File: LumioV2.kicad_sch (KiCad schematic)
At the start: 56 parts, among them J1 I2C POINT 1 - QWIIC, J10 MOTOR B, J11 Analog Input, J12 Analog Input, J13 Analog Input, J14 Analog Input, J15 Analog Input, J16 Analog Input, J17 Analog Input, J18 Analog Input, J2 I2C POINT 2 - QWIIC, J3 I2C POINT 3 - JST-PH, J4 I2C POINT 4 - JST-PH, J5 Raspi 5, J6 US Dist - Front, J7 US Dist - Back, J8 Display Connector, J9 MOTOR A, U1 LM2577T-ADJ/NOPB, U2 L298N, U3 MCP3008

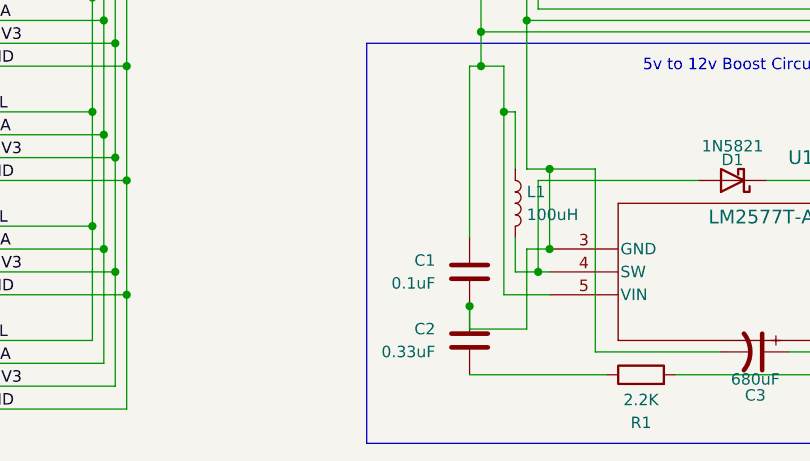
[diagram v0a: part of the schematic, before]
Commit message: added all footprints to schematics, also added all footprints to the pcb what's left: layout and routing
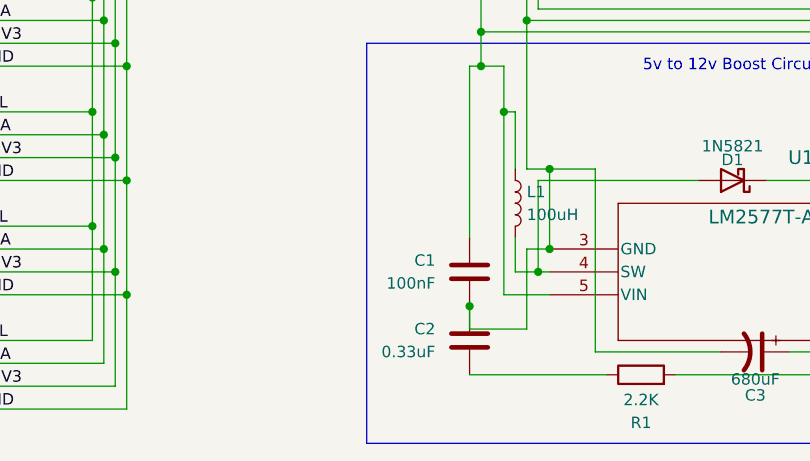
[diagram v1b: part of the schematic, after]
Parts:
- C1: value 0.1uF -> 100nF; footprint Capacitor_SMD:C_0603_1608Metric -> Capacitor_SMD:C_0402_1005Metric_Pad0.74x0.62mm_HandSolder
- C10, C11, C12, C13, C14, C15, C16, C17, C18, C19, C2, C20, C21, C22, C23, C24, C4, C5, C6, C7, C8, C9: footprint Capacitor_SMD:C_0603_1608Metric -> Capacitor_SMD:C_0402_1005Metric_Pad0.74x0.62mm_HandSolder
- D2, D3, D4, D5, D6, D7, D8, D9: value 1N4148WT -> SS34B; footprint Diode_SMD:D_SOD-523 -> Diode_SMD:D_SMA_Handsoldering
- J10, J9: footprint (none) -> TerminalBlock:TerminalBlock_MaiXu_MX126-5.0-02P_1x02_P5.00mm
- J11, J12, J13, J14, J15, J16, J17, J18: footprint (none) -> Connector_PinHeader_2.54mm:PinHeader_1x03_P2.54mm_Vertical
- J5: footprint Connector_PinHeader_1.00mm:PinHeader_2x20_P1.00mm_Vertical -> Connector_PinHeader_2.54mm:PinHeader_2x20_P2.54mm_Vertical
- J6, J7: footprint (none) -> Connector_PinHeader_2.54mm:PinHeader_1x04_P2.54mm_Vertical
- J8: footprint (none) -> Connector_PinHeader_2.54mm:PinHeader_2x13_P2.54mm_Vertical
- L1: footprint (none) -> Inductor_THT:L_Radial_D21.0mm_P19.00mm
- R1: footprint (none) -> Resistor_SMD:R_0805_2012Metric_Pad1.20x1.40mm_HandSolder
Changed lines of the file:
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@@
 			)
 		)
-		(property "Footprint" "Capacitor_SMD:C_0603_1608Metric"
+		(property "Footprint" "Capacitor_SMD:C_0402_1005Metric_Pad0.74x0.62mm_HandSolder"
 			(at 31.75 166.37 0)
 			(effects
@@
 			)
 		)
-		(property "Footprint" ""
+		(property "Footprint" "TerminalBlock:TerminalBlock_MaiXu_MX126-5.0-02P_1x02_P5.00mm"
 			(at 251.46 147.32 0)
 			(effects
@@
 			)
 		)
-		(property "Footprint" "Capacitor_SMD:C_0603_1608Metric"
+		(property "Footprint" "Capacitor_SMD:C_0402_1005Metric_Pad0.74x0.62mm_HandSolder"
 			(at 250.19 44.45 0)
 			(effects
@@
 			)
 		)
-		(property "Value" "1N4148WT"
+		(property "Value" "SS34B"
 			(at 243.84 139.7 90)
 			(effects
@@
 			)
 		)
-		(property "Footprint" "Diode_SMD:D_SOD-523"
+		(property "Footprint" "Diode_SMD:D_SMA_Handsoldering"
 			(at 234.315 132.08 0)
 			(effects
@@
 			)
 		)
-		(property "Footprint" "Capacitor_SMD:C_0603_1608Metric"
+		(property "Footprint" "Capacitor_SMD:C_0402_1005Metric_Pad0.74x0.62mm_HandSolder"
 			(at 101.6 31.75 0)
 			(effects
@@
 			)
 		)
-		(property "Footprint" "Capacitor_SMD:C_0603_1608Metric"
+		(property "Footprint" "Capacitor_SMD:C_0402_1005Metric_Pad0.74x0.62mm_HandSolder"
 			(at 199.0852 127 0)
 			(effects
@@
 			)
 		)
-		(property "Footprint" "Capacitor_SMD:C_0603_1608Metric"
+		(property "Footprint" "Capacitor_SMD:C_0402_1005Metric_Pad0.74x0.62mm_HandSolder"
 			(at 173.99 92.71 0)
 			(effects
@@
 			)
 		)
-		(property "Value" "1N4148WT"
+		(property "Value" "SS34B"
 			(at 238.76 165.1 90)
 			(effects
@@
 			)
 		)
-		(property "Footprint" "Diode_SMD:D_SOD-523"
+		(property "Footprint" "Diode_SMD:D_SMA_Handsoldering"
 			(at 229.235 157.48 0)
 			(effects
@@
 			)
 		)
-		(property "Value" "1N4148WT"
+		(property "Value" "SS34B"
 			(at 233.68 165.1 90)
 			(effects
@@
 			)
 		)
-		(property "Footprint" "Diode_SMD:D_SOD-523"
+		(property "Footprint" "Diode_SMD:D_SMA_Handsoldering"
 			(at 224.155 157.48 0)
 			(effects
@@
 			)
 		)
-		(property "Value" "0.1uF"
+		(property "Value" "100nF"
 			(at 101.6 177.7999 0)
 			(effects
@@
 			)
 		)
-		(property "Footprint" "Capacitor_SMD:C_0603_1608Metric"
+		(property "Footprint" "Capacitor_SMD:C_0402_1005Metric_Pad0.74x0.62mm_HandSolder"
 			(at 104.4448 180.34 0)
 			(effects
@@
 			)
 		)
-		(property "Footprint" ""
+		(property "Footprint" "Connector_PinHeader_2.54mm:PinHeader_1x03_P2.54mm_Vertical"
 			(at 241.3 54.61 0)
 			(effects
@@
 			)
 		)
-		(property "Footprint" "Connector_PinHeader_1.00mm:PinHeader_2x20_P1.00mm_Vertical"
+		(property "Footprint" "Connector_PinHeader_2.54mm:PinHeader_2x20_P2.54mm_Vertical"
 			(at 90.17 81.28 0)
 			(effects
@@
 			)
 		)
-		(property "Footprint" "Capacitor_SMD:C_0603_1608Metric"
+		(property "Footprint" "Capacitor_SMD:C_0402_1005Metric_Pad0.74x0.62mm_HandSolder"
 			(at 213.0552 127 0)
 			(effects
@@
 			)
 		)
-		(property "Footprint" "Capacitor_SMD:C_0603_1608Metric"
+		(property "Footprint" "Capacitor_SMD:C_0402_1005Metric_Pad0.74x0.62mm_HandSolder"
 			(at 31.75 191.77 0)
 			(effects
@@
 			)
 		)
-		(property "Footprint" ""
+		(property "Footprint" "Connector_PinHeader_2.54mm:PinHeader_1x03_P2.54mm_Vertical"
 			(at 227.33 39.37 0)
 			(effects
@@
 			)
 		)
-		(property "Footprint" "Capacitor_SMD:C_0603_1608Metric"
+		(property "Footprint" "Capacitor_SMD:C_0402_1005Metric_Pad0.74x0.62mm_HandSolder"
 			(at 236.22 59.69 0)
 			(effects
@@
 			)
 		)
-		(property "Footprint" "Capacitor_SMD:C_0603_1608Metric"
+		(property "Footprint" "Capacitor_SMD:C_0402_1005Metric_Pad0.74x0.62mm_HandSolder"
 			(at 121.92 31.75 0)
 			(effects
@@
 			)
 		)
-		(property "Footprint" "Capacitor_SMD:C_0603_1608Metric"
+		(property "Footprint" "Capacitor_SMD:C_0402_1005Metric_Pad0.74x0.62mm_HandSolder"
 			(at 31.75 179.07 0)
 			(effects
@@
 			)
 		)
-		(property "Value" "1N4148WT"
+		(property "Value" "SS34B"
 			(at 243.84 165.1 90)
 			(effects
@@
 			)
 		)
-		(property "Footprint" "Diode_SMD:D_SOD-523"
+		(property "Footprint" "Diode_SMD:D_SMA_Handsoldering"
 			(at 234.315 157.48 0)
 			(effects
@@
 			)
 		)
-		(property "Footprint" "Capacitor_SMD:C_0603_1608Metric"
+		(property "Footprint" "Capacitor_SMD:C_0402_1005Metric_Pad0.74x0.62mm_HandSolder"
 			(at 121.92 74.93 0)
 			(effects
@@
 			)
 		)
-		(property "Footprint" ""
+		(property "Footprint" "Connector_PinHeader_2.54mm:PinHeader_1x03_P2.54mm_Vertical"
 			(at 241.3 39.37 0)
 			(effects
@@
 			)
 		)
-		(property "Footprint" "Capacitor_SMD:C_0603_1608Metric"
+		(property "Footprint" "Capacitor_SMD:C_0402_1005Metric_Pad0.74x0.62mm_HandSolder"
 			(at 222.25 44.45 0)
 			(effects
@@
 			)
 		)
-		(property "Footprint" ""
+		(property "Footprint" "Connector_PinHeader_2.54mm:PinHeader_1x04_P2.54mm_Vertical"
 			(at 95.25 25.4 0)
 			(effects
@@
 			)
 		)
-		(property "Footprint" "Capacitor_SMD:C_0603_1608Metric"
+		(property "Footprint" "Capacitor_SMD:C_0402_1005Metric_Pad0.74x0.62mm_HandSolder"
 			(at 222.25 59.69 0)
 			(effects
@@
 			)
 		)
-		(property "Value" "1N4148WT"
+		(property "Value" "SS34B"
 			(at 228.6 165.1 90)
 			(effects
@@
 			)
 		)
-		(property "Footprint" "Diode_SMD:D_SOD-523"
+		(property "Footprint" "Diode_SMD:D_SMA_Handsoldering"
 			(at 219.075 157.48 0)
 			(effects
@@
 			)
 		)
-		(property "Footprint" ""
+		(property "Footprint" "Connector_PinHeader_2.54mm:PinHeader_1x03_P2.54mm_Vertical"
 			(at 213.36 39.37 0)
 			(effects
@@
 			)
 		)
-		(property "Value" "1N4148WT"
+		(property "Value" "SS34B"
 			(at 233.68 139.7 90)
 			(effects
@@
 			)
 		)
-		(property "Footprint" "Diode_SMD:D_SOD-523"
+		(property "Footprint" "Diode_SMD:D_SMA_Handsoldering"
 			(at 224.155 132.08 0)
 			(effects
@@
 			)
 		)
-		(property "Footprint" ""
+		(property "Footprint" "Connector_PinHeader_2.54mm:PinHeader_1x03_P2.54mm_Vertical"
 			(at 255.27 39.37 0)
 			(effects
@@
 			)
 		)
-		(property "Footprint" "Capacitor_SMD:C_0603_1608Metric"
+		(property "Footprint" "Capacitor_SMD:C_0402_1005Metric_Pad0.74x0.62mm_HandSolder"
 			(at 31.75 153.67 0)
 			(effects
@@
 			)
 		)
-		(property "Footprint" "Capacitor_SMD:C_0603_1608Metric"
+		(property "Footprint" "Capacitor_SMD:C_0402_1005Metric_Pad0.74x0.62mm_HandSolder"
 			(at 207.01 44.45 0)
 			(effects
@@
 			)
 		)
-		(property "Footprint" ""
+		(property "Footprint" "Resistor_SMD:R_0805_2012Metric_Pad1.20x1.40mm_HandSolder"
 			(at 124.46 189.738 90)
 			(effects
@@
 			)
 		)
-		(property "Footprint" "Capacitor_SMD:C_0603_1608Metric"
+		(property "Footprint" "Capacitor_SMD:C_0402_1005Metric_Pad0.74x0.62mm_HandSolder"
 			(at 148.59 66.04 0)
 			(effects
@@
 			)
 		)
-		(property "Footprint" "Capacitor_SMD:C_0603_1608Metric"
+		(property "Footprint" "Capacitor_SMD:C_0402_1005Metric_Pad0.74x0.62mm_HandSolder"
 			(at 104.4448 187.96 0)
 			(effects
@@
 			)
 		)
-		(property "Footprint" ""
+		(property "Footprint" "Connector_PinHeader_2.54mm:PinHeader_1x03_P2.54mm_Vertical"
 			(at 213.36 54.61 0)
 			(effects
@@
 			)
 		)
-		(property "Footprint" "Capacitor_SMD:C_0603_1608Metric"
+		(property "Footprint" "Capacitor_SMD:C_0402_1005Metric_Pad0.74x0.62mm_HandSolder"
 			(at 139.7 64.77 0)
 			(effects
@@
 			)
 		)
-		(property "Footprint" ""
+		(property "Footprint" "Connector_PinHeader_2.54mm:PinHeader_1x04_P2.54mm_Vertical"
 			(at 115.57 25.4 0)
 			(effects
@@
 			)
 		)
-		(property "Footprint" "Capacitor_SMD:C_0603_1608Metric"
+		(property "Footprint" "Capacitor_SMD:C_0402_1005Metric_Pad0.74x0.62mm_HandSolder"
 			(at 181.61 92.71 0)
 			(effects
@@
 			)
 		)
-		(property "Footprint" "Capacitor_SMD:C_0603_1608Metric"
+		(property "Footprint" "Capacitor_SMD:C_0402_1005Metric_Pad0.74x0.62mm_HandSolder"
 			(at 250.19 59.69 0)
 			(effects
@@
 			)
 		)
-		(property "Footprint" "Capacitor_SMD:C_0603_1608Metric"
+		(property "Footprint" "Capacitor_SMD:C_0402_1005Metric_Pad0.74x0.62mm_HandSolder"
 			(at 236.22 44.45 0)
 			(effects
@@
 			)
 		)
-		(property "Value" "1N4148WT"
+		(property "Value" "SS34B"
 			(at 238.76 139.7 90)
 			(effects
@@
 			)
 		)
-		(property "Footprint" "Diode_SMD:D_SOD-523"
+		(property "Footprint" "Diode_SMD:D_SMA_Handsoldering"
 			(at 229.235 132.08 0)
 			(effects
@@
 			)
 		)
-		(property "Footprint" ""
+		(property "Footprint" "Connector_PinHeader_2.54mm:PinHeader_1x03_P2.54mm_Vertical"
 			(at 227.33 54.61 0)
 			(effects
@@
 			)
 		)
-		(property "Value" "1N4148WT"
+		(property "Value" "SS34B"
 			(at 228.6 139.7 90)
 			(effects
@@
 			)
 		)
-		(property "Footprint" "Diode_SMD:D_SOD-523"
+		(property "Footprint" "Diode_SMD:D_SMA_Handsoldering"
 			(at 219.075 132.08 0)
 			(effects
@@
 			)
 		)
-		(property "Footprint" "Capacitor_SMD:C_0603_1608Metric"
+		(property "Footprint" "Capacitor_SMD:C_0402_1005Metric_Pad0.74x0.62mm_HandSolder"
 			(at 208.28 59.69 0)
 			(effects
@@
 			)
 		)
-		(property "Footprint" ""
+		(property "Footprint" "Inductor_THT:L_Radial_D21.0mm_P19.00mm"
 			(at 110.49 168.91 0)
 			(effects
@@
 			)
 		)
-		(property "Footprint" ""
+		(property "Footprint" "Connector_PinHeader_2.54mm:PinHeader_1x03_P2.54mm_Vertical"
 			(at 255.27 54.61 0)
 			(effects
@@
 			)
 		)
-		(property "Footprint" ""
+		(property "Footprint" "Connector_PinHeader_2.54mm:PinHeader_2x13_P2.54mm_Vertical"
 			(at 133.35 87.63 0)
 			(effects
@@
 			)
 		)
-		(property "Footprint" ""
+		(property "Footprint" "TerminalBlock:TerminalBlock_MaiXu_MX126-5.0-02P_1x02_P5.00mm"
 			(at 251.46 139.7 0)
 			(effects

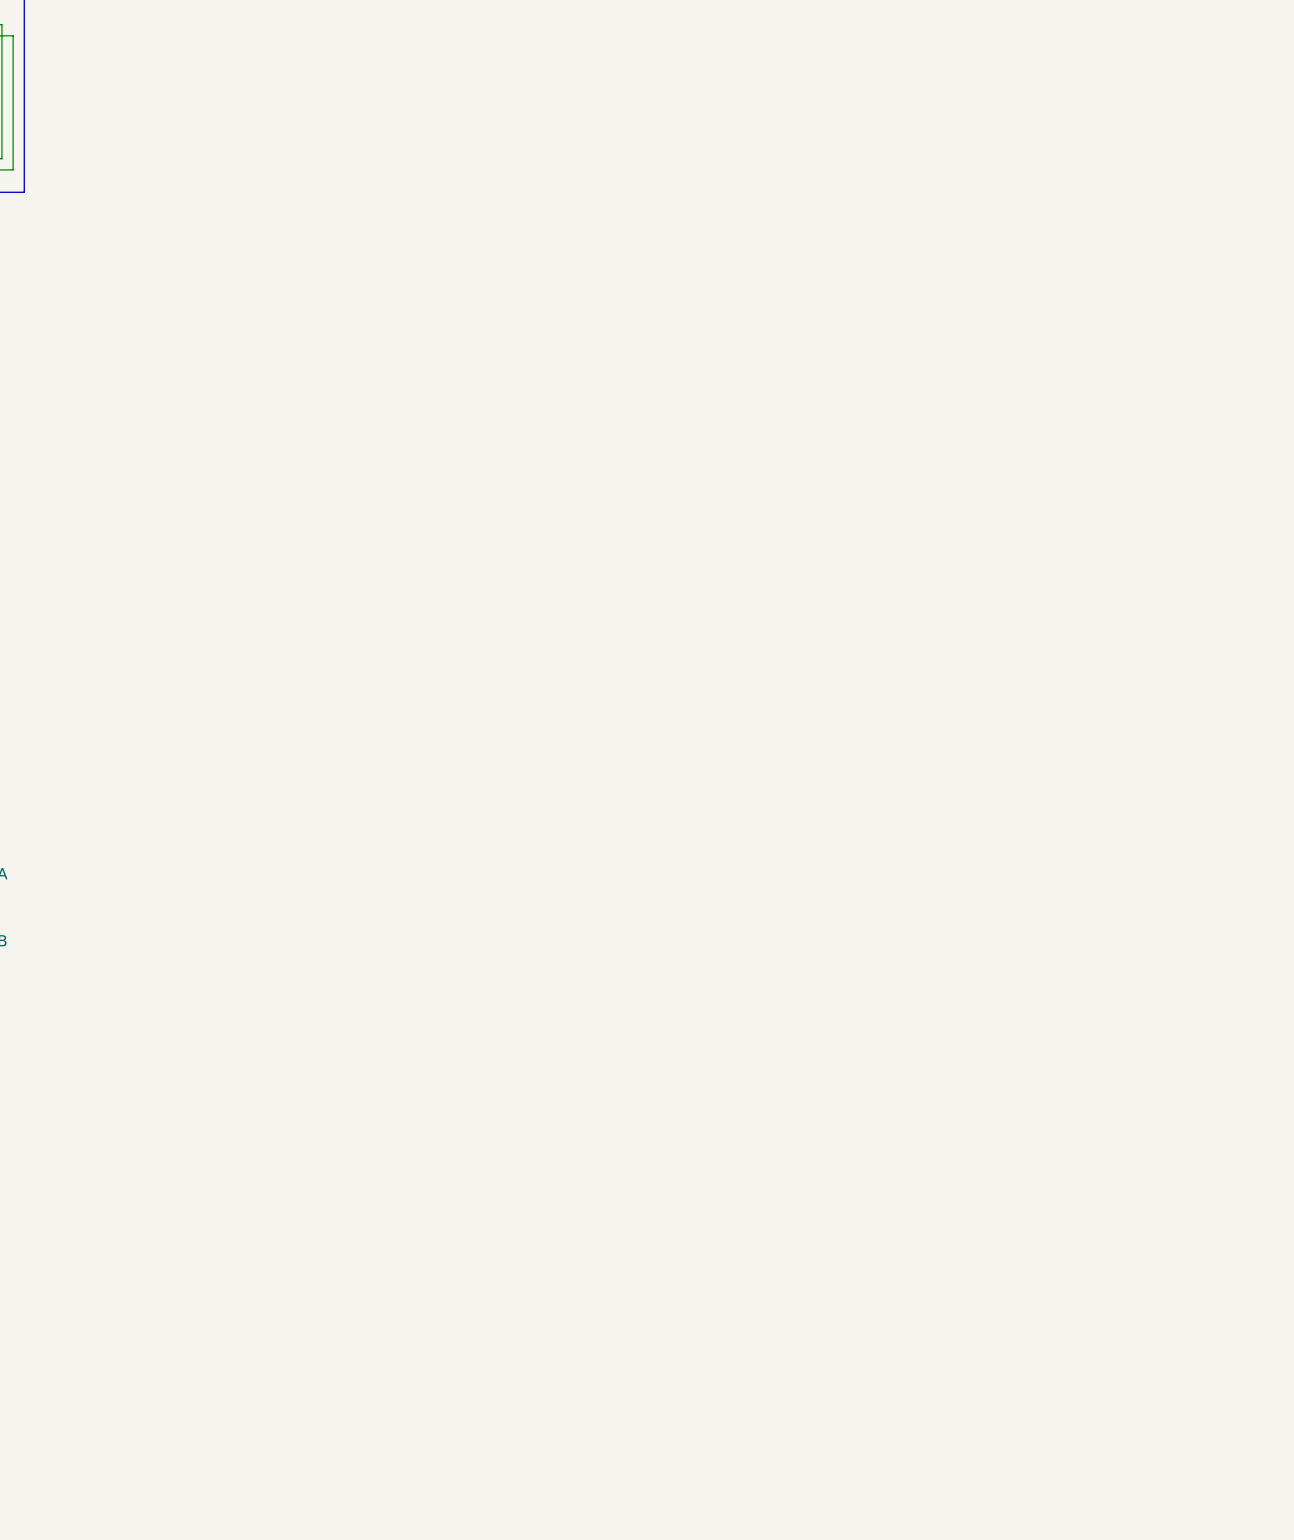
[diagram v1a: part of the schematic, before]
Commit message: Added rp2040 slave for extra gpios and current and voltage monitor
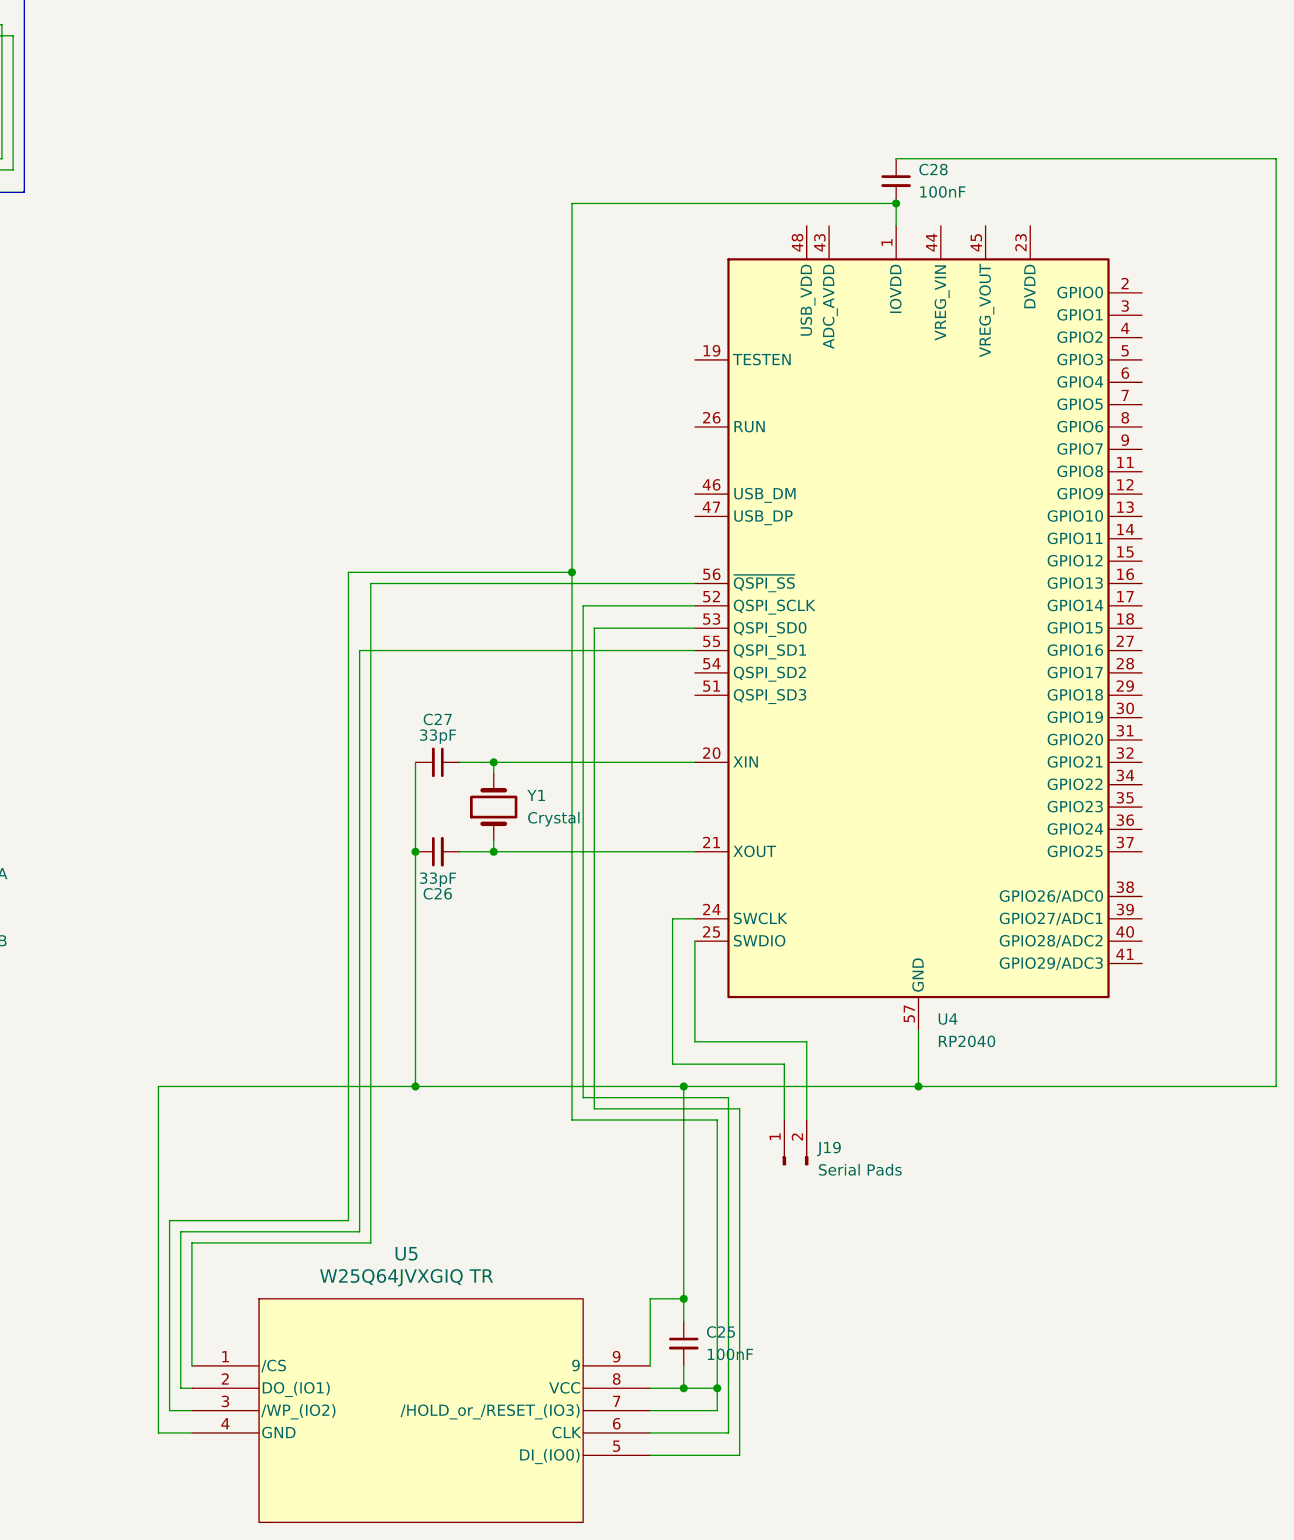
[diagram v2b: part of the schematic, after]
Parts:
- added C25, C28: 100nF, symbol Device:C_Small
- added C26, C27: 33pF, symbol Device:C_Small
- added J19: Serial Pads, symbol Connector:Conn_01x02_Pin
- added U4: RP2040, Package_DFN_QFN:QFN-56-1EP_7x7mm_P0.4mm_EP3.2x3.2mm, symbol MCU_RaspberryPi:RP2040
- added U5: W25Q64JVXGIQ TR, Package_DFN_QFN:DFN-8-1EP_6x5mm_P1.27mm_EP4x4mm, symbol W25Q64JVXGIQ:W25Q64JVXGIQ_TR
- added Y1: Crystal, Crystal:Crystal_SMD_HC49-SD, symbol Device:Crystal
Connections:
- new net: U4.56 (~{QSPI_SS}), U5.1 (/CS)
- new net: U4.55 (QSPI_SD1), U5.2 (DO_(IO1))
- new net: C25.2, C28.2, U4.1 (IOVDD), U4.10 (IOVDD), U4.22 (IOVDD), U4.33 (IOVDD), U4.42 (IOVDD), U4.49 (IOVDD), U5.3 (/WP_(IO2)), U5.7 (/HOLD_or_/RESET_(IO3)), U5.8 (VCC)
- new net: C25.1, C26.1, C27.2, C28.1, U4.57 (GND), U5.4 (GND), U5.9
- new net: U4.53 (QSPI_SD0), U5.5 (DI_(IO0))
- new net: U4.52 (QSPI_SCLK), U5.6 (CLK)
- new net: C27.1, U4.20 (XIN), Y1.2
- new net: C26.2, U4.21 (XOUT), Y1.1
- new net: J19.1 (Pin_1), U4.24 (SWCLK)
- new net: J19.2 (Pin_2), U4.25 (SWDIO)
- new net: U4.23 (DVDD), U4.50 (DVDD)
